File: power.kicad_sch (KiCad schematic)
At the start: 12 parts, among them U2 TPS562202, U3 LM7806_TO220

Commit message: feat: led_inf connected, load cell overvoltage protection and antenna vals defined
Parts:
- L1: value L -> 3.6uH
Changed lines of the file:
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@@
 		)
 	)
-	(label "MCU 3.3 VCC"
+	(label "MCU 6 VCC"
 		(at 80.01 71.12 0)
 		(effects
@@
 			)
 		)
-		(property "Value" "L"
+		(property "Value" "3.6uH"
 			(at 152.4 30.48 90)
 			(effects

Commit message: feat: added power button, name changes
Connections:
- no-connect marks 1 -> 0
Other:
- note added: "3.3 V power converter"
- note added: "6 V power converter"
- note added: "Power switch"

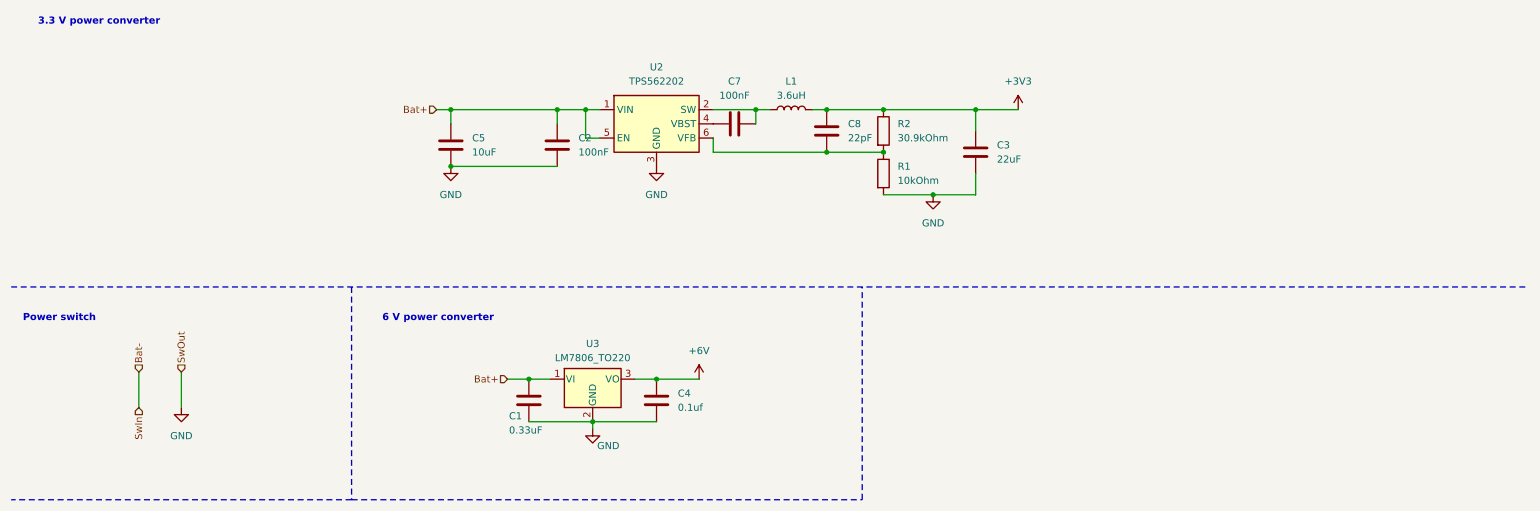
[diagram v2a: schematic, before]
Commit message: feat: pcb almost done, added rgb led
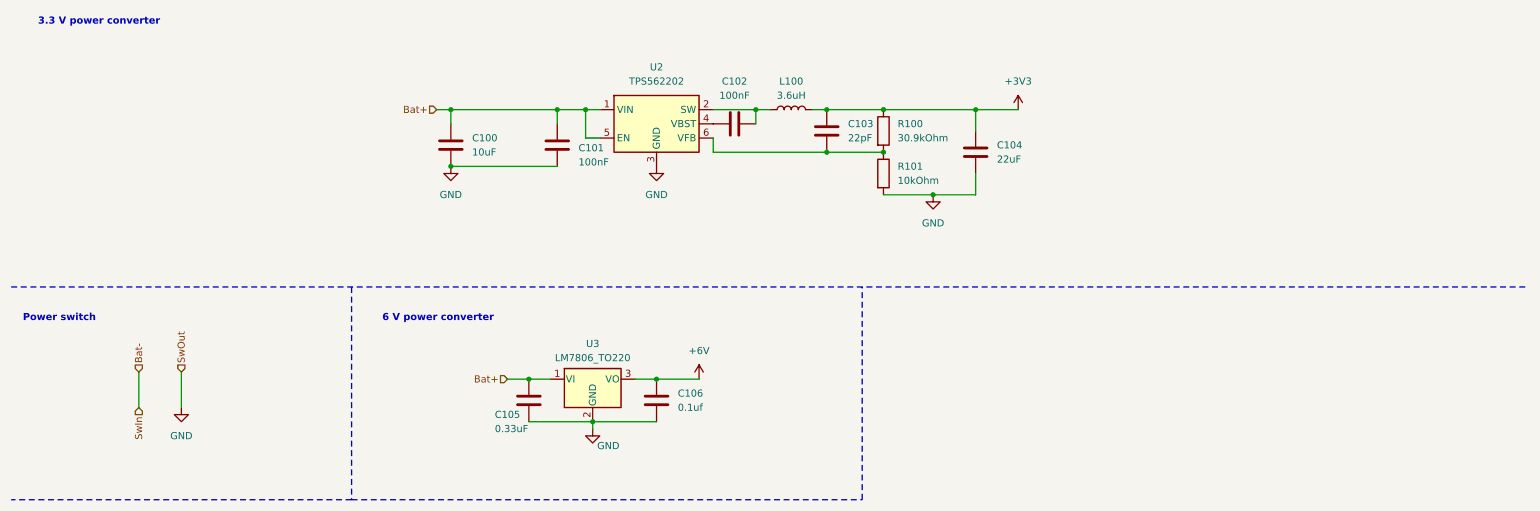
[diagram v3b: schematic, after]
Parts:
- renumbered C5 to C100, C2 to C101, C7 to C102, C8 to C103, C3 to C104, C1 to C105, C4 to C106, L1 to L100, R2 to R100, R1 to R101
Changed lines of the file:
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@@
 	(generator_version "9.0")
 	(paper "A4")
+	(title_block
+		(date "2025-12-08")
+	)
 	(text "6 V power converter"
 		(exclude_from_sim no)
@@
 		(dnp no)
 		(fields_autoplaced yes)
-		(property "Reference" "C4"
+		(property "Reference" "C106"
 			(at 132.08 83.8199 0)
 			(effects
@@
 			(project "maszyna_do_nalewania"
 				(path "/9edf3a40-33ab-40a8-8c54-e53c70f0a44f/44c20dfa-9471-4f9b-af92-d8f9ab961a4f"
-					(reference "C4")
+					(reference "C106")
 					(unit 1)
 				)
@@
 		(on_board yes)
 		(dnp no)
-		(property "Reference" "C8"
+		(property "Reference" "C103"
 			(at 162.56 35.5599 0)
 			(effects
@@
 			(project ""
 				(path "/9edf3a40-33ab-40a8-8c54-e53c70f0a44f/44c20dfa-9471-4f9b-af92-d8f9ab961a4f"
-					(reference "C8")
+					(reference "C103")
 					(unit 1)
 				)
@@
 		(on_board yes)
 		(dnp no)
-		(property "Reference" "C1"
-			(at 101.854 87.884 0)
+		(property "Reference" "C105"
+			(at 99.314 87.63 0)
 			(effects
 				(font
@@
 		)
 		(property "Value" "0.33uF"
-			(at 101.854 90.424 0)
+			(at 99.314 90.17 0)
 			(effects
 				(font
@@
 			(project ""
 				(path "/9edf3a40-33ab-40a8-8c54-e53c70f0a44f/44c20dfa-9471-4f9b-af92-d8f9ab961a4f"
-					(reference "C1")
+					(reference "C105")
 					(unit 1)
 				)
@@
 		(on_board yes)
 		(dnp no)
-		(property "Reference" "C5"
+		(property "Reference" "C100"
 			(at 95.25 38.0999 0)
 			(effects
@@
 			(project ""
 				(path "/9edf3a40-33ab-40a8-8c54-e53c70f0a44f/44c20dfa-9471-4f9b-af92-d8f9ab961a4f"
-					(reference "C5")
+					(reference "C100")
 					(unit 1)
 				)
@@
 		(dnp no)
 		(fields_autoplaced yes)
-		(property "Reference" "L1"
+		(property "Reference" "L100"
 			(at 152.4 27.94 90)
 			(effects
@@
 			(project ""
 				(path "/9edf3a40-33ab-40a8-8c54-e53c70f0a44f/44c20dfa-9471-4f9b-af92-d8f9ab961a4f"
-					(reference "L1")
+					(reference "L100")
 					(unit 1)
 				)
@@
 		(dnp no)
 		(fields_autoplaced yes)
-		(property "Reference" "C3"
+		(property "Reference" "C104"
 			(at 189.23 39.3699 0)
 			(effects
@@
 			(project ""
 				(path "/9edf3a40-33ab-40a8-8c54-e53c70f0a44f/44c20dfa-9471-4f9b-af92-d8f9ab961a4f"
-					(reference "C3")
+					(reference "C104")
 					(unit 1)
 				)
@@
 		(dnp no)
 		(fields_autoplaced yes)
-		(property "Reference" "R1"
+		(property "Reference" "R101"
 			(at 171.45 43.1799 0)
 			(effects
@@
 			(project ""
 				(path "/9edf3a40-33ab-40a8-8c54-e53c70f0a44f/44c20dfa-9471-4f9b-af92-d8f9ab961a4f"
-					(reference "R1")
+					(reference "R101")
 					(unit 1)
 				)
@@
 		(dnp no)
 		(fields_autoplaced yes)
-		(property "Reference" "C7"
+		(property "Reference" "C102"
 			(at 142.24 27.94 90)
 			(effects
@@
 			(project ""
 				(path "/9edf3a40-33ab-40a8-8c54-e53c70f0a44f/44c20dfa-9471-4f9b-af92-d8f9ab961a4f"
-					(reference "C7")
+					(reference "C102")
 					(unit 1)
 				)
@@
 		(on_board yes)
 		(dnp no)
-		(fields_autoplaced yes)
-		(property "Reference" "C2"
-			(at 114.3 38.0999 0)
+		(property "Reference" "C101"
+			(at 114.3 39.878 0)
 			(effects
 				(font
@@
 		)
 		(property "Value" "100nF"
-			(at 114.3 40.6399 0)
+			(at 114.3 42.418 0)
 			(effects
 				(font
@@
 			(project ""
 				(path "/9edf3a40-33ab-40a8-8c54-e53c70f0a44f/44c20dfa-9471-4f9b-af92-d8f9ab961a4f"
-					(reference "C2")
+					(reference "C101")
 					(unit 1)
 				)
@@
 		(dnp no)
 		(fields_autoplaced yes)
-		(property "Reference" "R2"
+		(property "Reference" "R100"
 			(at 171.45 35.5599 0)
 			(effects
@@
 			(project ""
 				(path "/9edf3a40-33ab-40a8-8c54-e53c70f0a44f/44c20dfa-9471-4f9b-af92-d8f9ab961a4f"
-					(reference "R2")
-					(unit 1)
-				)
+					(reference "R100")
+					(unit 1)
+				)

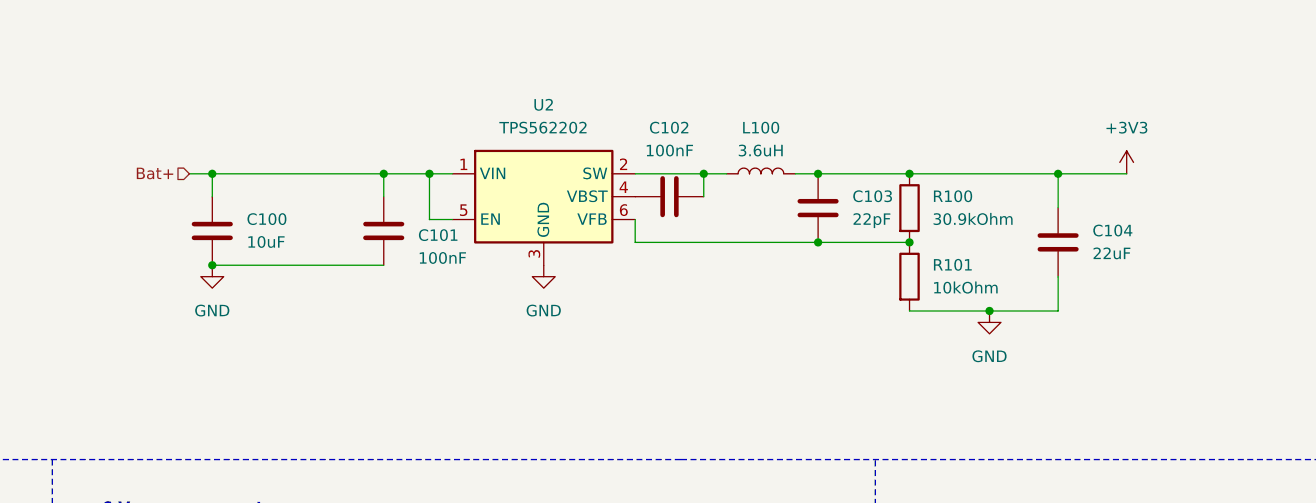
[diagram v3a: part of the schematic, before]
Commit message: feat: silkscreen done
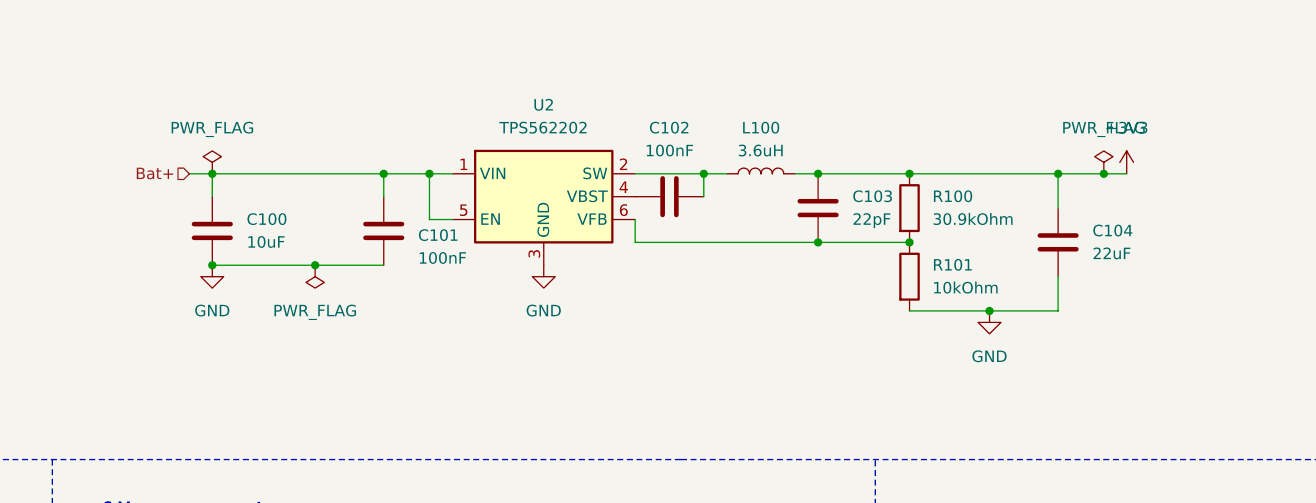
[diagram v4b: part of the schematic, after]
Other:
- company: (none) -> Mateusz Drogowski Karol Dworczyński
- title: (none) -> Drink Pouring Machine - Power Subsystem
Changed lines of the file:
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@@
 	(paper "A4")
 	(title_block
+		(title "Drink Pouring Machine - Power Subsystem")
 		(date "2025-12-08")
+		(rev "v1.0")
+		(company "Mateusz Drogowski Karol Dworczyński")
 	)
 	(text "6 V power converter"
@@
 	)
 	(junction
+		(at 190.5 33.02)
+		(diameter 0)
+		(color 0 0 0 0)
+	)
+	(junction
 		(at 91.44 43.18)
 		(diameter 0)
@@
 	)
 	(junction
+		(at 102.87 43.18)
+		(diameter 0)
+		(color 0 0 0 0)
+	)
+	(junction
 		(at 105.41 81.28)
 		(diameter 0)
@@
 	(wire
 		(pts
-			(xy 185.42 33.02) (xy 193.04 33.02)
+			(xy 185.42 33.02) (xy 190.5 33.02)
 		)
 		(stroke
@@
 		)
 	)
+	(wire
+		(pts
+			(xy 102.87 43.18) (xy 110.49 43.18)
+		)
+		(stroke
+			(width 0)
+			(type default)
+		)
+	)
 	(polyline
 		(pts
@@
 	(wire
 		(pts
+			(xy 190.5 33.02) (xy 193.04 33.02)
+		)
+		(stroke
+			(width 0)
+			(type default)
+		)
+	)
+	(wire
+		(pts
 			(xy 138.43 38.1) (xy 138.43 40.64)
 		)
@@
 	(wire
 		(pts
-			(xy 91.44 43.18) (xy 110.49 43.18)
+			(xy 91.44 43.18) (xy 102.87 43.18)
 		)
 		(stroke
@@
 	)
 	(symbol
+		(lib_id "power:PWR_FLAG")
+		(at 190.5 33.02 0)
+		(unit 1)
+		(exclude_from_sim no)
+		(in_bom yes)
+		(on_board yes)
+		(dnp no)
+		(fields_autoplaced yes)
+		(property "Reference" "#FLG02"
+			(at 190.5 31.115 0)
+			(effects
+				(font
+					(size 1.27 1.27)
+				)
+				(hide yes)
+			)
+		)
+		(property "Value" "PWR_FLAG"
+			(at 190.5 27.94 0)
+			(effects
+				(font
+					(size 1.27 1.27)
+				)
+			)
+		)
+		(property "Footprint" ""
+			(at 190.5 33.02 0)
+			(effects
+				(font
+					(size 1.27 1.27)
+				)
+				(hide yes)
+			)
+		)
+		(property "Datasheet" "~"
+			(at 190.5 33.02 0)
+			(effects
+				(font
+					(size 1.27 1.27)
+				)
+				(hide yes)
+			)
+		)
+		(property "Description" "Special symbol for telling ERC where power comes from"
+			(at 190.5 33.02 0)
+			(effects
+				(font
+					(size 1.27 1.27)
+				)
+				(hide yes)
+			)
+		)
+		(pin "1"
+		)
+		(instances
+			(project ""
+				(path "/9edf3a40-33ab-40a8-8c54-e53c70f0a44f/44c20dfa-9471-4f9b-af92-d8f9ab961a4f"
+					(reference "#FLG02")
+					(unit 1)
+				)
+			)
+		)
+	)
+	(symbol
 		(lib_id "power:GND")
 		(at 91.44 43.18 0)
@@
 	)
 	(symbol
+		(lib_id "power:PWR_FLAG")
+		(at 91.44 33.02 0)
+		(unit 1)
+		(exclude_from_sim no)
+		(in_bom yes)
+		(on_board yes)
+		(dnp no)
+		(fields_autoplaced yes)
+		(property "Reference" "#FLG01"
+			(at 91.44 31.115 0)
+			(effects
+				(font
+					(size 1.27 1.27)
+				)
+				(hide yes)
+			)
+		)
+		(property "Value" "PWR_FLAG"
+			(at 91.44 27.94 0)
+			(effects
+				(font
+					(size 1.27 1.27)
+				)
+			)
+		)
+		(property "Footprint" ""
+			(at 91.44 33.02 0)
+			(effects
+				(font
+					(size 1.27 1.27)
+				)
+				(hide yes)
+			)
+		)
+		(property "Datasheet" "~"
+			(at 91.44 33.02 0)
+			(effects
+				(font
+					(size 1.27 1.27)
+				)
+				(hide yes)
+			)
+		)
+		(property "Description" "Special symbol for telling ERC where power comes from"
+			(at 91.44 33.02 0)
+			(effects
+				(font
+					(size 1.27 1.27)
+				)
+				(hide yes)
+			)
+		)
+		(pin "1"
+		)
+		(instances
+			(project ""
+				(path "/9edf3a40-33ab-40a8-8c54-e53c70f0a44f/44c20dfa-9471-4f9b-af92-d8f9ab961a4f"
+					(reference "#FLG01")
+					(unit 1)
+				)
+			)
+		)
+	)
+	(symbol
 		(lib_id "Device:C")
 		(at 185.42 40.64 0)
@@
 					(unit 1)
 				)
+			)
+		)
+	)
+	(symbol
+		(lib_id "power:PWR_FLAG")
+		(at 102.87 43.18 180)
+		(unit 1)
+		(exclude_from_sim no)
+		(in_bom yes)
+		(on_board yes)
+		(dnp no)
+		(fields_autoplaced yes)
+		(property "Reference" "#FLG03"
+			(at 102.87 45.085 0)
+			(effects
+				(font
+					(size 1.27 1.27)
+				)
+				(hide yes)
+			)
+		)
+		(property "Value" "PWR_FLAG"
+			(at 102.87 48.26 0)
+			(effects
+				(font
+					(size 1.27 1.27)
+				)
+			)
+		)
+		(property "Footprint" ""
+			(at 102.87 43.18 0)
+			(effects
+				(font
+					(size 1.27 1.27)
+				)
+				(hide yes)
+			)
+		)
+		(property "Datasheet" "~"
+			(at 102.87 43.18 0)
+			(effects
+				(font
+					(size 1.27 1.27)
+				)
+				(hide yes)
+			)
+		)
+		(property "Description" "Special symbol for telling ERC where power comes from"
+			(at 102.87 43.18 0)
+			(effects
+				(font
+					(size 1.27 1.27)
+				)
+				(hide yes)
+			)
+		)
+		(pin "1"
+		)
+		(instances
+			(project ""
+				(path "/9edf3a40-33ab-40a8-8c54-e53c70f0a44f/44c20dfa-9471-4f9b-af92-d8f9ab961a4f"
+					(reference "#FLG03")
+					(unit 1)
+				)

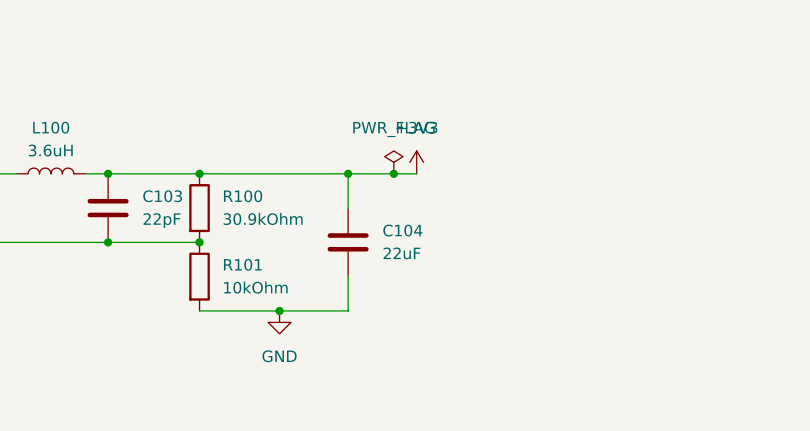
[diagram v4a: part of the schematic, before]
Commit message: fix: led resistor values, tensometer screw terminal
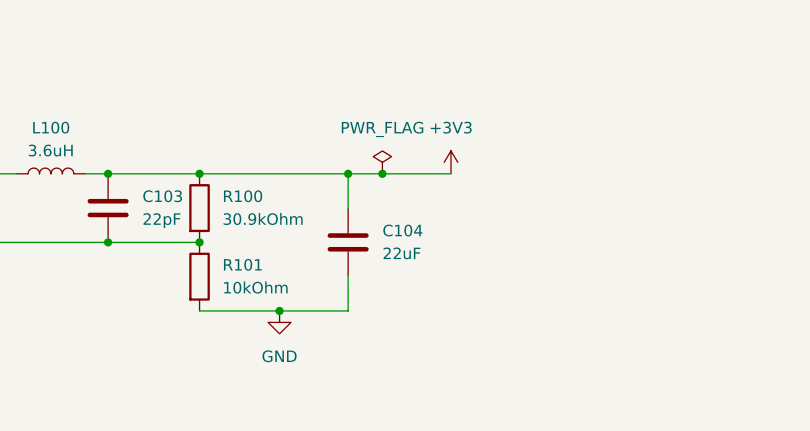
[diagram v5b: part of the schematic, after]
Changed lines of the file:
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@@
+	)
+	(junction
+		(at 189.23 33.02)
+		(diameter 0)
+		(color 0 0 0 0)
 	)
 	(junction
@@
 	)
 	(junction
-		(at 190.5 33.02)
-		(diameter 0)
-		(color 0 0 0 0)
-	)
-	(junction
 		(at 91.44 43.18)
 		(diameter 0)
@@
 	(wire
 		(pts
-			(xy 185.42 33.02) (xy 190.5 33.02)
+			(xy 185.42 33.02) (xy 189.23 33.02)
 		)
 		(stroke
@@
 		)
 	)
+	(wire
+		(pts
+			(xy 189.23 33.02) (xy 196.85 33.02)
+		)
+		(stroke
+			(width 0)
+			(type default)
+		)
+	)
 	(polyline
 		(pts
@@
 		(pts
 			(xy 116.84 88.9) (xy 116.84 90.17)
-		)
-		(stroke
-			(width 0)
-			(type default)
-		)
-	)
-	(wire
-		(pts
-			(xy 190.5 33.02) (xy 193.04 33.02)
 		)
 		(stroke
@@
 	(symbol
 		(lib_id "power:PWR_FLAG")
-		(at 190.5 33.02 0)
+		(at 189.23 33.02 0)
 		(unit 1)
 		(exclude_from_sim no)
@@
 		(fields_autoplaced yes)
 		(property "Reference" "#FLG02"
-			(at 190.5 31.115 0)
+			(at 189.23 31.115 0)
 			(effects
 				(font
@@
 		)
 		(property "Value" "PWR_FLAG"
-			(at 190.5 27.94 0)
+			(at 189.23 27.94 0)
 			(effects
 				(font
@@
 		)
 		(property "Footprint" ""
-			(at 190.5 33.02 0)
+			(at 189.23 33.02 0)
 			(effects
 				(font
@@
 		)
 		(property "Datasheet" "~"
-			(at 190.5 33.02 0)
+			(at 189.23 33.02 0)
 			(effects
 				(font
@@
 		)
 		(property "Description" "Special symbol for telling ERC where power comes from"
-			(at 190.5 33.02 0)
+			(at 189.23 33.02 0)
 			(effects
 				(font
@@
 	(symbol
 		(lib_id "power:+3V3")
-		(at 193.04 33.02 0)
+		(at 196.85 33.02 0)
 		(unit 1)
 		(exclude_from_sim no)
@@
 		(fields_autoplaced yes)
 		(property "Reference" "#PWR06"
-			(at 193.04 36.83 0)
+			(at 196.85 36.83 0)
 			(effects
 				(font
@@
 		)
 		(property "Value" "+3V3"
-			(at 193.04 27.94 0)
+			(at 196.85 27.94 0)
 			(effects
 				(font
@@
 		)
 		(property "Footprint" ""
-			(at 193.04 33.02 0)
+			(at 196.85 33.02 0)
 			(effects
 				(font
@@
 		)
 		(property "Datasheet" ""
-			(at 193.04 33.02 0)
+			(at 196.85 33.02 0)
 			(effects
 				(font
@@
 		)
 		(property "Description" "Power symbol creates a global label with name \"+3V3\""
-			(at 193.04 33.02 0)
-			(effects
-				(font
+			(at 196.85 33.02 0)
+			(effects
+				(font
